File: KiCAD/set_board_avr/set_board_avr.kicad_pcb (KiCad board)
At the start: 2 copper layers, 197.5 x 12.7 mm, 34 parts, among them J1 Conn_01x10, J2 AVR-ISP-6, Q1 Q_NPN, Q2 Q_NPN, Q3 Q_NPN, U1 ATtiny4313-S, U4 74HC14, U5 NCP1117-3.3_SOT223, Y1 ASV-xxxMHz

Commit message: working on routing
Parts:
- removed C4: 1.0uF, Capacitor_SMD:C_1206_3216Metric_Pad1.33x1.80mm_HandSolder
- moved R14 5.13 mm to (124.6, 28.5), turned to 0 degrees
- moved C5 3.39 mm to (102.6, 30.4), turned to 0 degrees
- moved C6 3.16 mm to (143.8, 28.6), turned to 0 degrees
- moved D2 3.13 mm to (167.5, 33.9)
- moved D3 3.13 mm to (167.5, 37.7)
- moved R12 3.13 mm to (161.5, 33.9)
- moved R13 3.13 mm to (161.5, 37.7)
- moved D1 3.13 mm to (167.5, 30.0)
- moved R11 3.13 mm to (161.5, 30.1)
- moved C7 2.41 mm to (151.3, 28.7)
- moved Y1 1.40 mm to (151.3, 36.0)
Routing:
- net +3.3V: track 0.00 -> 207.5 mm, vias 0 -> 10
- net Net-(J1-Pin_6): track 0.00 -> 61.2 mm, vias 0 -> 3
- net Net-(J1-Pin_5): track 0.00 -> 59.5 mm, vias 0 -> 3
- net Net-(J1-Pin_8): track 0.00 -> 58.6 mm, vias 0 -> 3
- net Net-(J1-Pin_7): track 0.00 -> 54.8 mm, vias 0 -> 3
- net Net-(J1-Pin_3): track 0.00 -> 40.6 mm, vias 0 -> 3
- net Net-(J1-Pin_4): track 0.00 -> 35.4 mm, vias 0 -> 5
- net Net-(J1-Pin_2): track 0.00 -> 26.7 mm, vias 0 -> 2
- net +12V: track 0.00 -> 14.4 mm, vias 0 -> 2
- added copper zone on F.Cu, net GND
- removed copper zone on B.Cu, net GND
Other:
- board size 197.5 x 12.7 mm -> 197.5 x 17.8 mm

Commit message: routed
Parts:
- moved D1 136.5 mm to (31.5, 41.8), turned to 0 degrees
- moved R11 125.1 mm to (36.9, 41.8), turned to 180 degrees
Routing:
- net Net-(U1-PB2): track 0.00 -> 90.1 mm, vias 0 -> 4
- net Net-(U1-PB1): track 0.00 -> 86.0 mm, vias 0 -> 4
- net Net-(U1-PD5): track 0.00 -> 85.4 mm, vias 0 -> 4
- net Net-(U1-PB0): track 0.00 -> 83.1 mm, vias 0 -> 2
- net Net-(U1-PD0): track 0.00 -> 76.5 mm, vias 0 -> 3
- net Net-(U1-PD6): track 0.00 -> 68.8 mm, vias 0 -> 4
- net Net-(U1-PD1): track 0.00 -> 65.4 mm, vias 0 -> 3
- net Net-(U1-PB4): track 0.00 -> 65.1 mm, vias 0 -> 4
- net Net-(U1-PD3): track 0.00 -> 53.4 mm, vias 0 -> 4
- net Net-(U1-PD2): track 0.00 -> 52.2 mm, vias 0 -> 4
- net Net-(U1-PD4): track 0.00 -> 41.0 mm, vias 0 -> 4
- net /SCK: track 0.00 -> 33.8 mm, vias 0 -> 2
- net Net-(U1-PB3): track 0.00 -> 31.5 mm, vias 0 -> 4
- net /RST: track 0.00 -> 30.9 mm, vias 0 -> 2
- net /MISO: track 0.00 -> 29.3 mm
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- added copper zone on B.Cu, net GND

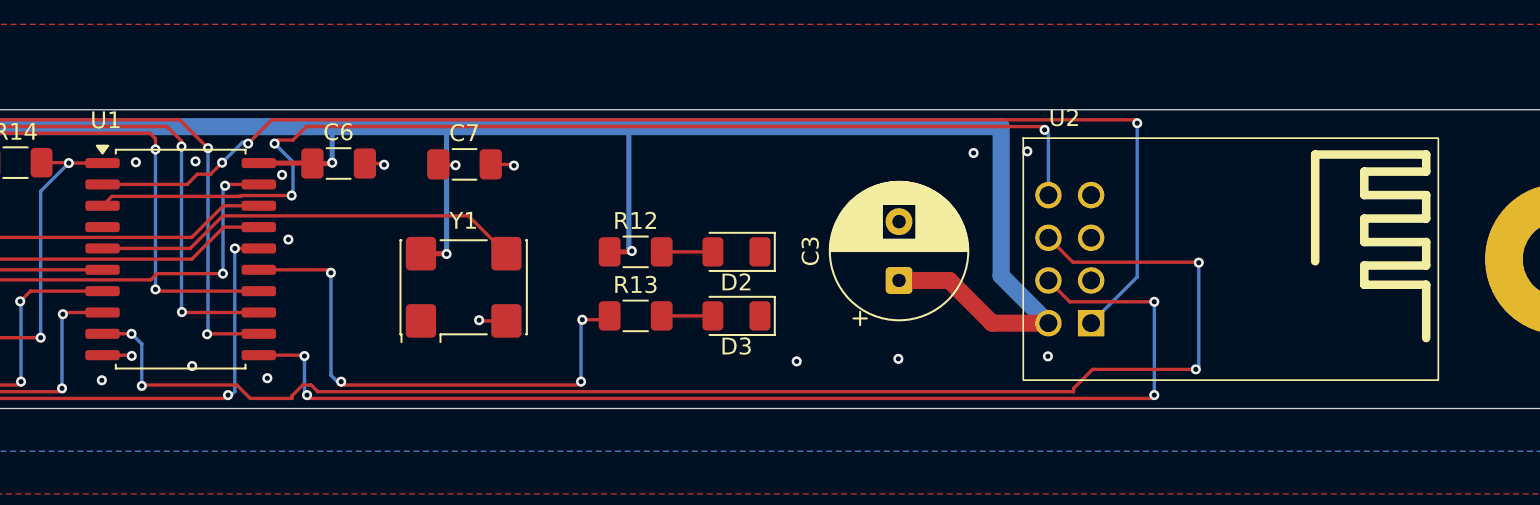
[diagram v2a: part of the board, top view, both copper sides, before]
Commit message: update for WWVB
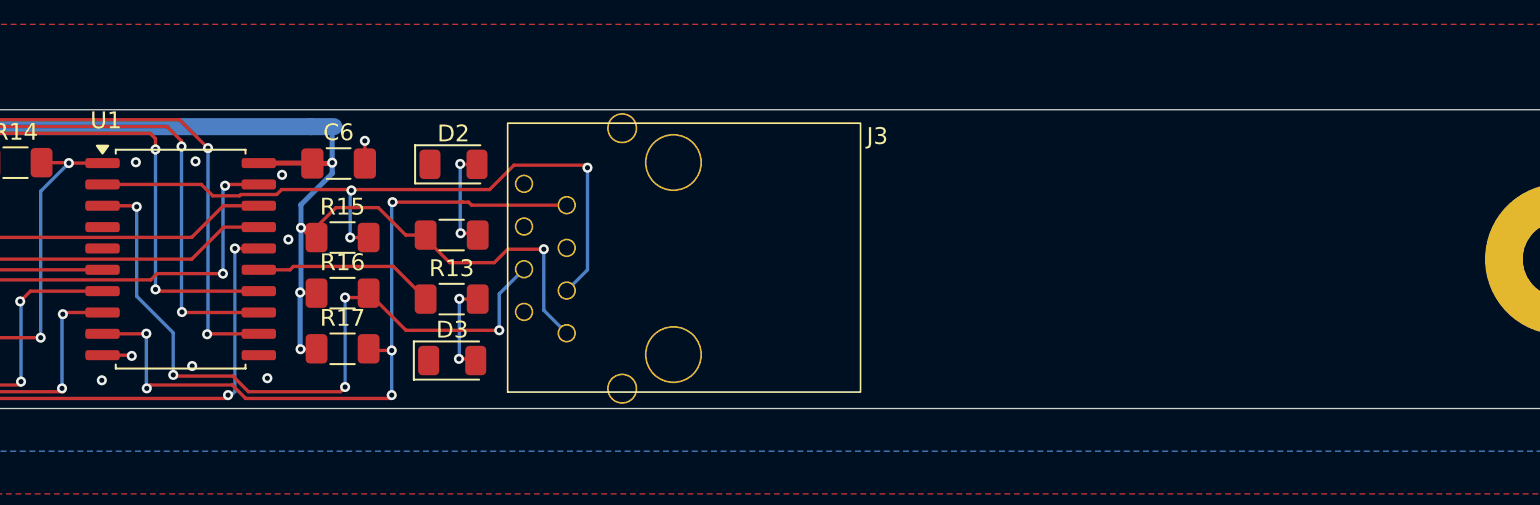
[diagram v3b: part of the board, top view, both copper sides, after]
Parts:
- removed C3: 470uF, Capacitor_THT:CP_Radial_D8.0mm_P3.50mm
- removed C7: 0.1uF, Capacitor_SMD:C_1206_3216Metric_Pad1.33x1.80mm_HandSolder
- removed U2: ~, my_wifi:ESP8266_Wifi_module
- removed Y1: ASV-xxxMHz, Oscillator:Oscillator_SMD_Abracon_ASV-4Pin_7.0x5.1mm
- added J3: RJ45, my_RJ45:Metz_AJT65B8813, F.Cu at (157.4, 38.7)
- added R15: 1k, Resistor_SMD:R_1206_3216Metric_Pad1.30x1.75mm_HandSolder, F.Cu at (144.1, 33.0)
- added R16: 1k, Resistor_SMD:R_1206_3216Metric_Pad1.30x1.75mm_HandSolder, F.Cu at (144.1, 36.3)
- added R17: 1k, Resistor_SMD:R_1206_3216Metric_Pad1.30x1.75mm_HandSolder, F.Cu at (144.1, 39.6)
- moved D2 17.6 mm to (150.7, 28.6), turned to 0 degrees
- moved D3 17.1 mm to (150.6, 40.3), turned to 0 degrees
- moved R12 11.0 mm to (150.5, 32.9)
- moved R13 11.0 mm to (150.5, 36.7)
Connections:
- U1 pad 11: Net-(U1-PD6) -> unconnected-(U1-PD6-Pad11)
- U1 pad 2: Net-(U1-PD0) -> /WWVB
- U1 pad 3: Net-(U1-PD1) -> /SPARE0
- U1 pad 5: Net-(U1-PA0/XTAL1) -> unconnected-(U1-PA0/XTAL1-Pad5)
- U1 pad 9: Net-(U1-PD5) -> /SPARE1
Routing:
- net Net-(U1-PD5): track 85.4 -> 0.00 mm, vias 4 -> 0
- net Net-(U1-PD0): track 76.5 -> 0.00 mm, vias 3 -> 0
- net Net-(U1-PD6): track 68.8 -> 0.00 mm, vias 4 -> 0
- net Net-(U1-PD1): track 65.4 -> 0.00 mm, vias 3 -> 0
- net +3.3V: track 208.9 -> 163.9 mm, vias 10 -> 11
- net /SPARE1: track 0.00 -> 44.6 mm, vias 0 -> 5
- net /SPARE0: track 0.00 -> 43.5 mm, vias 0 -> 5
- net /WWVB: track 0.00 -> 41.7 mm, vias 0 -> 3
- net Net-(U1-PA0/XTAL1): track 25.8 -> 0.00 mm
- net Net-(U1-PB3): track 31.5 -> 10.8 mm, vias 4 -> 0
- net Net-(D2-A): track 3.05 -> 6.21 mm, vias 0 -> 2
- net GND: track 9.77 -> 6.89 mm, vias 22 -> 15
- net Net-(D3-A): track 3.05 -> 5.89 mm, vias 0 -> 2

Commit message: finish place/route on set_board_avr
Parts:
- added C3: 100uF, Capacitor_THT:CP_Radial_D5.0mm_P2.00mm, F.Cu at (151.1, 28.6)
- added R18: 100, Resistor_SMD:R_1206_3216Metric_Pad1.30x1.75mm_HandSolder, F.Cu at (150.7, 33.5)
- moved D2 47.8 mm to (103.7, 37.5)
- moved R12 46.8 mm to (103.8, 34.3)
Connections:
- J3 pad 1: +3.3V -> Net-(C3-Pad1)
- R15 pad 1: +3.3V -> Net-(C3-Pad1)
- R16 pad 1: +3.3V -> Net-(C3-Pad1)
- R17 pad 1: +3.3V -> Net-(C3-Pad1)
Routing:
- net Net-(C3-Pad1): track 0.00 -> 33.7 mm, vias 0 -> 3
- net +3.3V: track 163.9 -> 143.0 mm, vias 11 -> 8
- net Net-(D2-A): track 6.21 -> 3.37 mm, vias 2 -> 0
- net GND: track 6.89 -> 7.81 mm, vias 15 -> 22
